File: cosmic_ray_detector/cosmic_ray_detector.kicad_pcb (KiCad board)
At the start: 4 copper layers, 80 x 60 mm, 56 parts, among them J1 MOLEX micro-fit 43045-0210, J2 5 pin pin header, J3 Black Banana, J4 Red Banana, J5 Green Banana, J6 BNC, U1 TL072, U2 TPS7A30, U3 TPS7A49, U4 TLV3501AIDBVTG4, U5 AD5270BRMZ-100-RL7

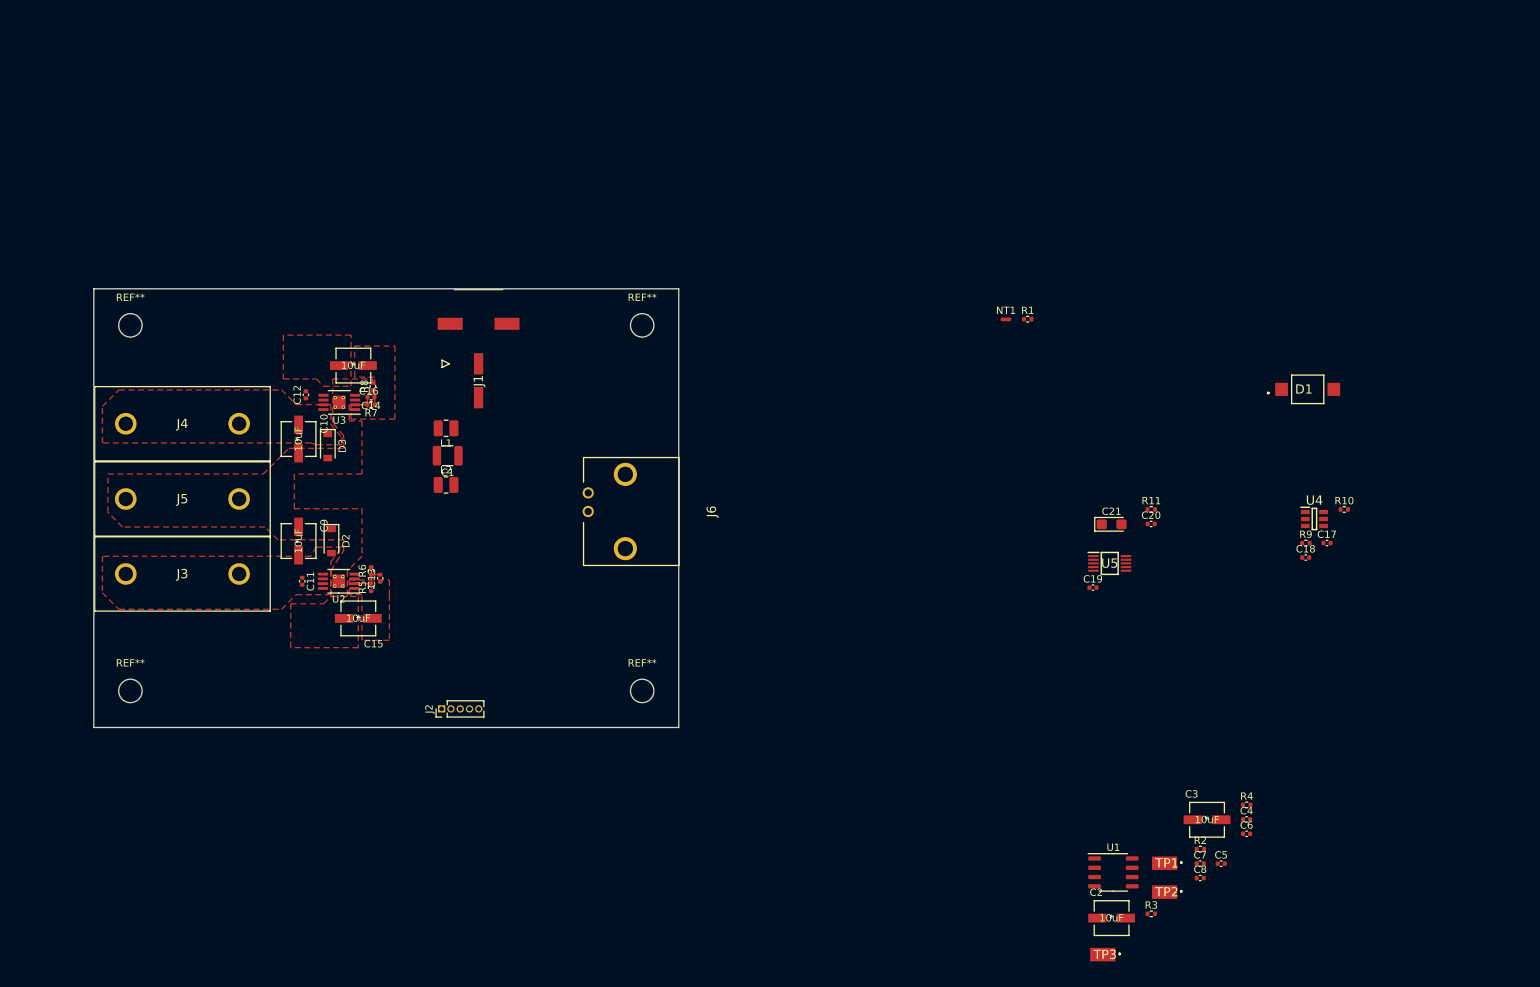
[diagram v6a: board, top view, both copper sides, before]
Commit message: changed a couple more caps
all components reasonably grouped, almost placed
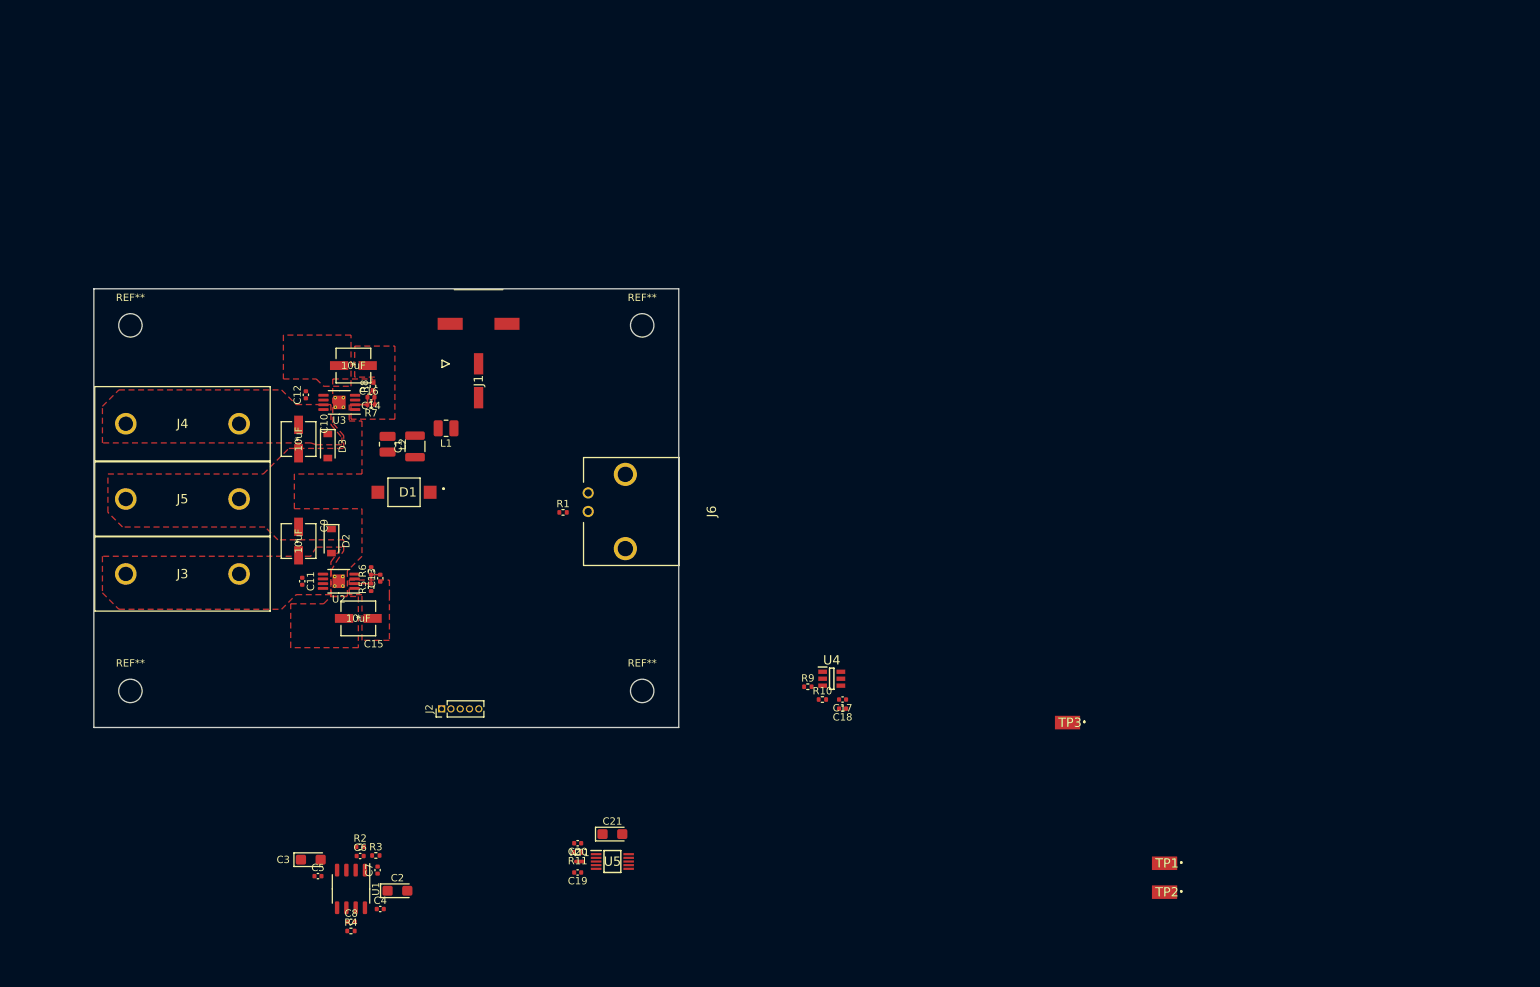
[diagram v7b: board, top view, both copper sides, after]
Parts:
- C2, C3: footprint cosmic_ray_detector_lib:MAL215375109E3 -> Capacitor_Tantalum_SMD:CP_EIA-3216-12_Kemet-S
- moved D1 124.4 mm to (102.5, 89.8), turned to 180 degrees
- moved R4 123.7 mm to (95.2, 149.8)
- moved C5 123.6 mm to (90.7, 142.2)
- moved C3 122.7 mm to (89.8, 140.0)
- moved C6 121.3 mm to (96.5, 139.5)
- moved C4 119.1 mm to (99.2, 146.8)
- moved C8 116.3 mm to (95.3, 148.5)
- moved R2 114.9 mm to (96.5, 138.2)
- moved C7 112.5 mm to (98.9, 141.4), turned to 90 degrees
- moved R3 106.4 mm to (98.6, 139.4)
- moved U1 104.3 mm to (95.2, 144.0), turned to -90 degrees
- moved C2 97.8 mm to (101.6, 144.2)
- moved NT1 94.3 mm to (126.5, 140.2)
- moved R11 91.4 mm to (126.2, 139.0), turned to 180 degrees
- moved C20 89.8 mm to (126.2, 137.8), turned to 180 degrees
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
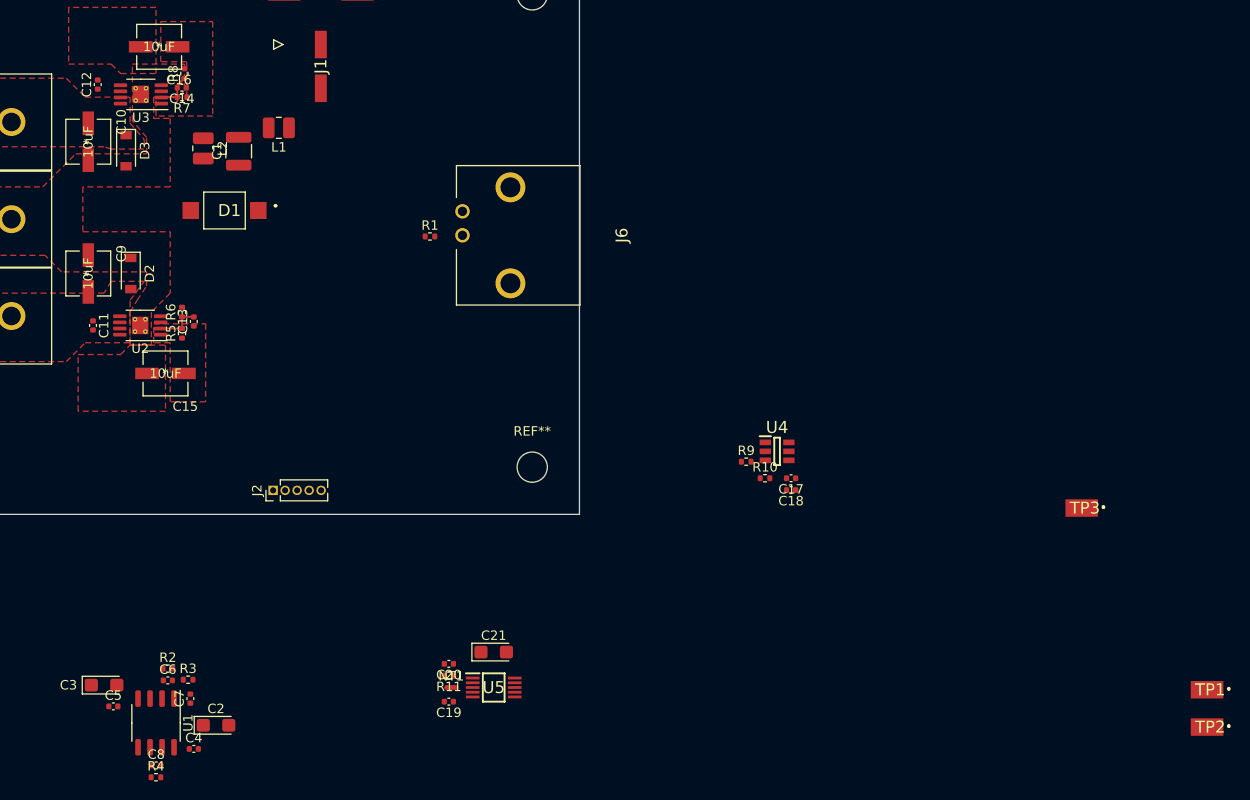
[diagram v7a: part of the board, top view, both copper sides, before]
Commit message: all placement done, slight tweaks, ready to route (I think)
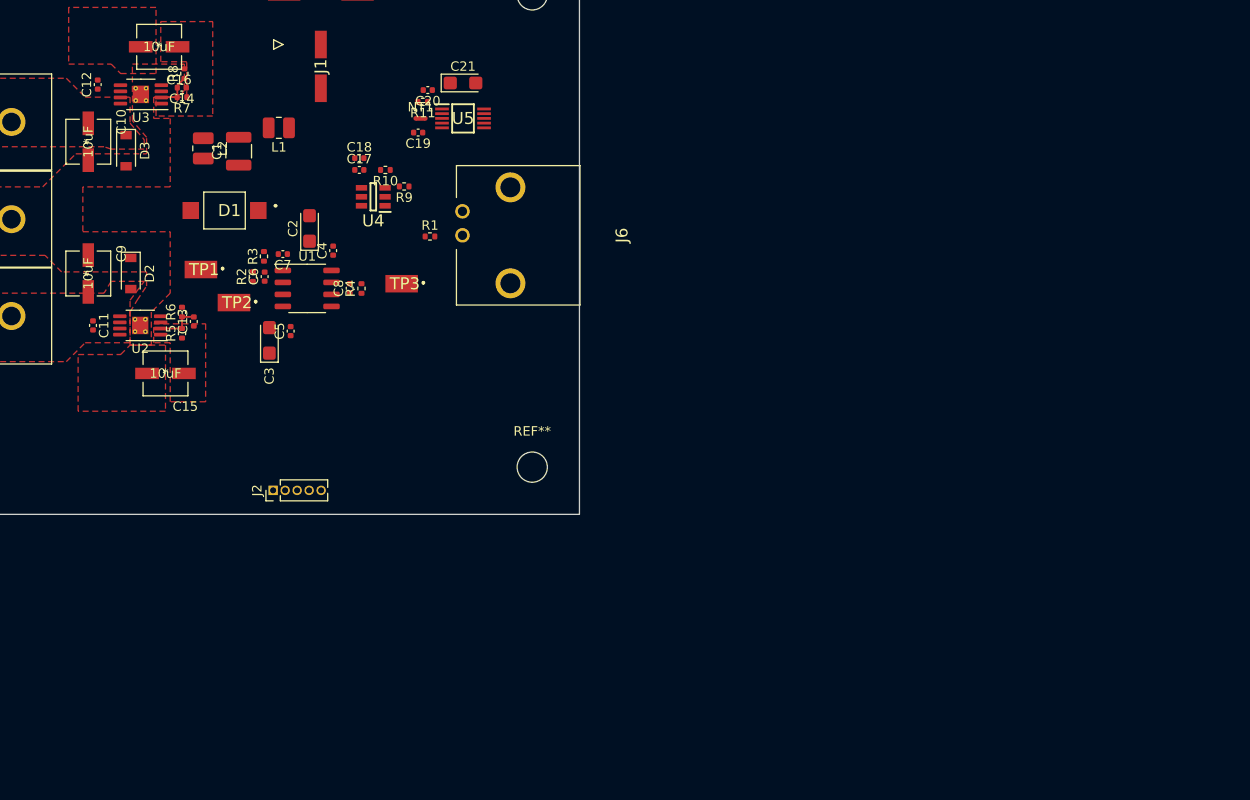
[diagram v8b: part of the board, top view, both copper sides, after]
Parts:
- moved TP1 115.4 mm to (100.0, 96.0)
- moved TP2 112.4 mm to (103.5, 99.5)
- moved TP3 75.8 mm to (121.2, 97.5)
- moved R11 60.8 mm to (123.5, 78.2)
- moved C20 60.8 mm to (124.0, 77.0)
- moved C19 60.3 mm to (123.0, 81.5)
- moved C21 60.3 mm to (127.8, 76.2)
- moved NT1 60.3 mm to (123.2, 80.0)
- moved U5 60.3 mm to (127.8, 80.0)
- moved C18 57.7 mm to (116.8, 84.2), turned to 0 degrees
- moved C17 56.2 mm to (116.8, 85.5), turned to 0 degrees
- moved R4 56.1 mm to (117.0, 98.0), turned to 90 degrees
- moved C4 54.8 mm to (114.0, 94.0), turned to 90 degrees
- moved C8 54.5 mm to (115.8, 98.0), turned to 90 degrees
- moved C2 53.5 mm to (111.5, 91.7), turned to 90 degrees
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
